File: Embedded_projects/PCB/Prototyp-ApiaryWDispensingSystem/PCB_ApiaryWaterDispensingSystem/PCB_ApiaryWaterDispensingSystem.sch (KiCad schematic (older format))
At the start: 0 parts

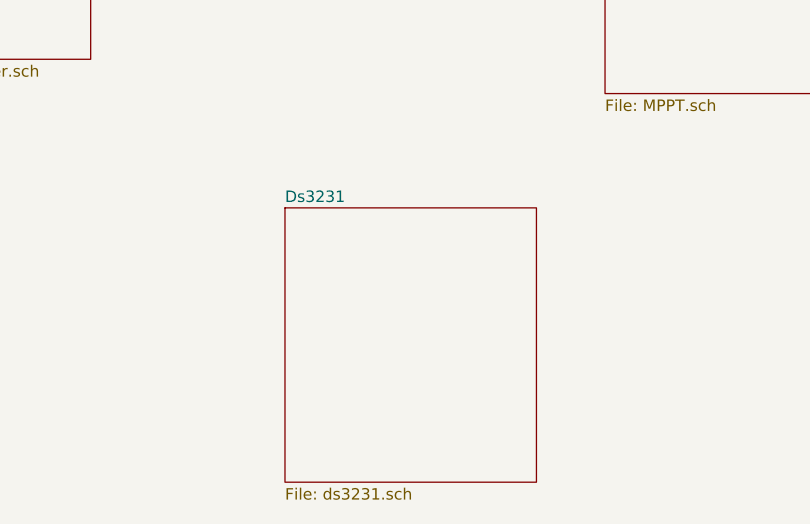
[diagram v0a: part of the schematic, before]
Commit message: added BME280 sensor to the project , #3
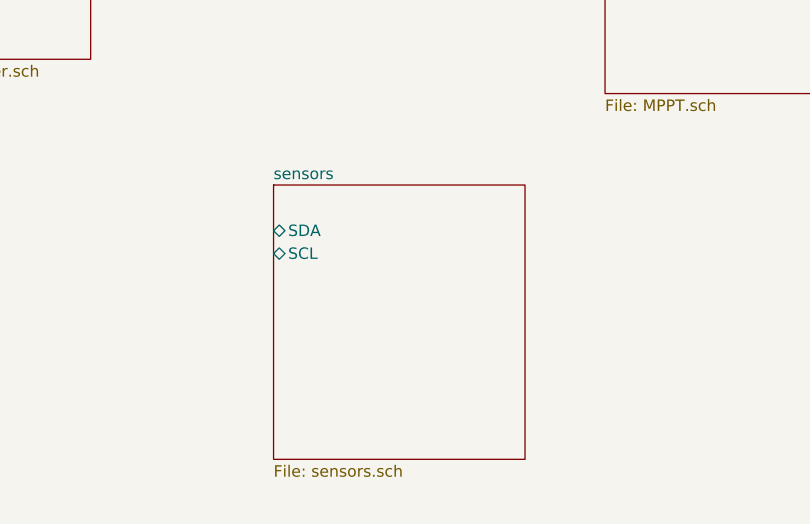
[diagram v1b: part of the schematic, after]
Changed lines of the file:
@@
 $EndSheet
 $Sheet
-S 4250 3850 1100 1200
+S 4200 3750 1100 1200
 U 67D47B32
-F0 "Ds3231" 50
-F1 "ds3231.sch" 50
+F0 "sensors" 50
+F1 "sensors.sch" 50
+F2 "SDA" B L 4200 3950 50
+F3 "SCL" B L 4200 4050 50
 $EndSheet
 $EndSCHEMATC

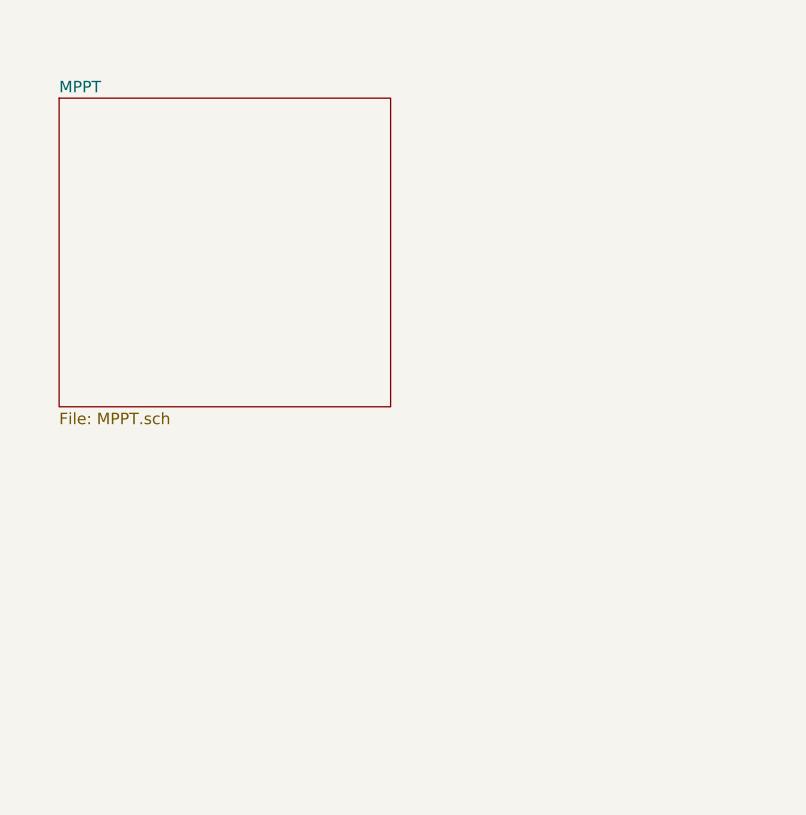
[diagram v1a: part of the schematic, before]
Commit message: added x-tal and his footprints for microcontroller schematics, user button
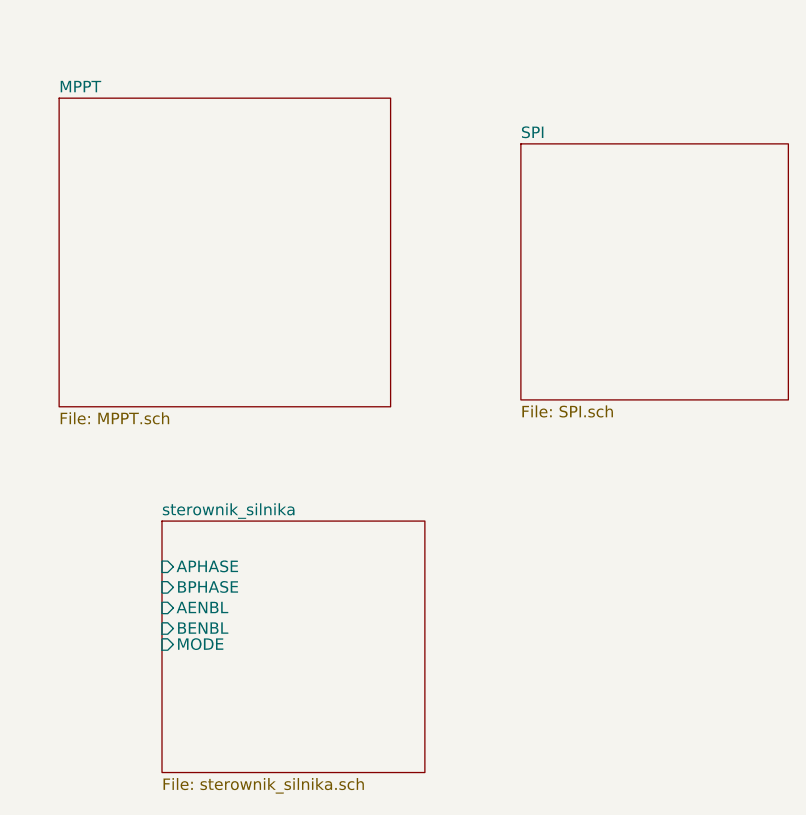
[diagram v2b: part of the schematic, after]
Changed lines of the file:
@@
 $Descr A4 11693 8268
 encoding utf-8
-Sheet 1 4
+Sheet 1 6
 Title ""
 Date ""
@@
 F3 "SCL" B L 4200 4050 50
 $EndSheet
+$Sheet
+S 6100 3850 1150 1100
+U 67E19E2D
+F0 "sterownik_silnika" 50
+F1 "sterownik_silnika.sch" 50
+F2 "APHASE" I L 6100 4050 50
+F3 "BPHASE" I L 6100 4140 50
+F4 "AENBL" I L 6100 4230 50
+F5 "BENBL" I L 6100 4320 50
+F6 "MODE" I L 6100 4390 50
+$EndSheet
+$Sheet
+S 7670 2200 1170 1120
+U 67E3C70E
+F0 "SPI" 50
+F1 "SPI.sch" 50
+$EndSheet
 $EndSCHEMATC

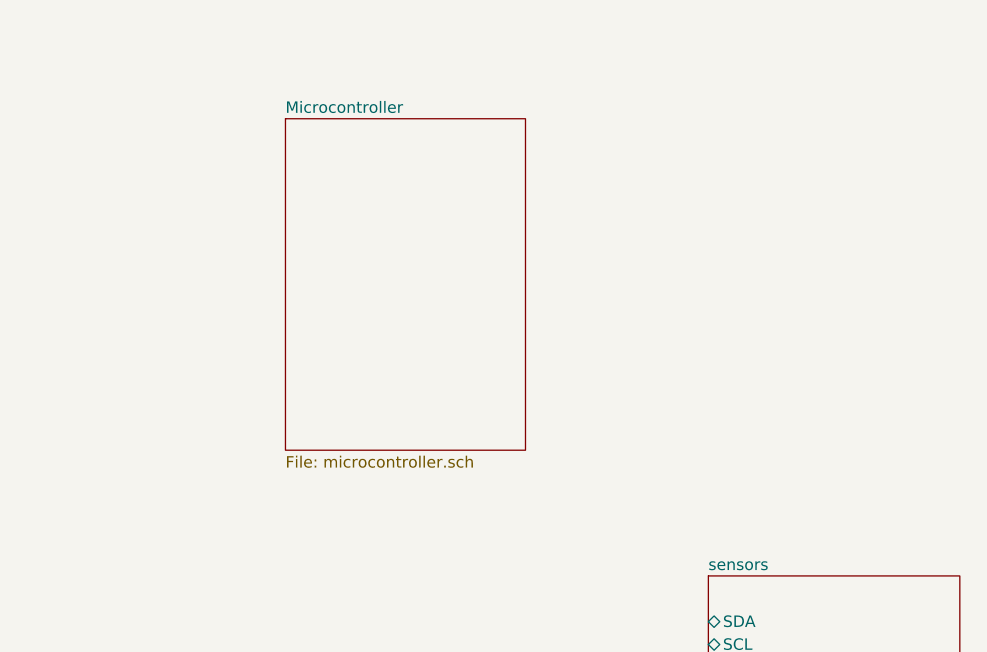
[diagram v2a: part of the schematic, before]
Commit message: stm32f411re completed schematic
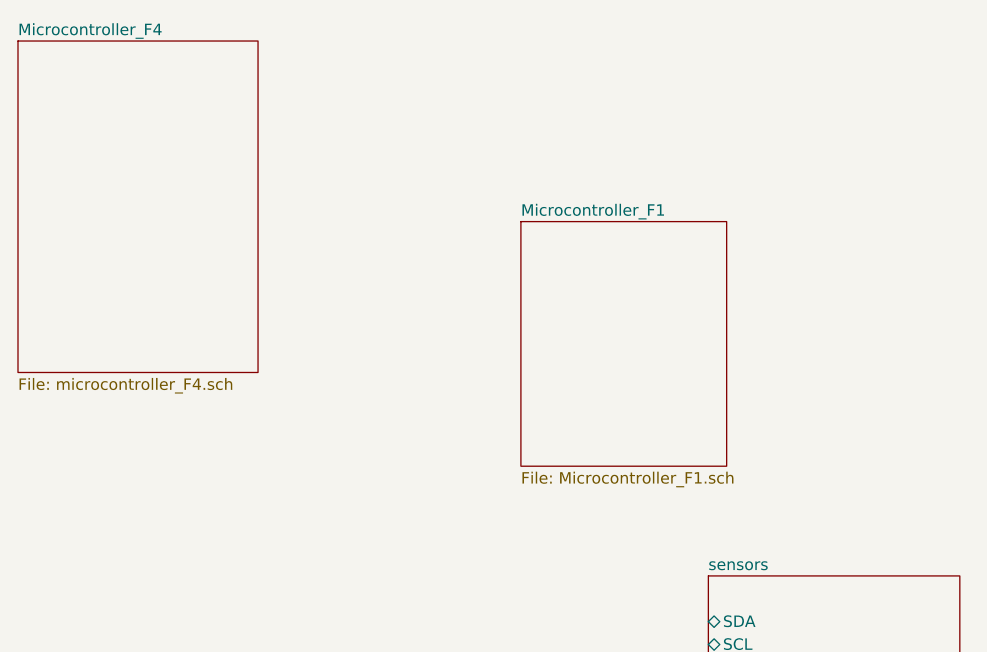
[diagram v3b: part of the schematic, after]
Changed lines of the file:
@@
 $Descr A4 11693 8268
 encoding utf-8
-Sheet 1 6
+Sheet 1 7
 Title ""
 Date ""
@@
 $EndDescr
 $Sheet
-S 2350 1750 1050 1450
+S 1180 1410 1050 1450
 U 67C77D26
-F0 "Microcontroller" 50
-F1 "microcontroller.sch" 50
+F0 "Microcontroller_F4" 50
+F1 "microcontroller_F4.sch" 50
 $EndSheet
 $Sheet
@@
 F1 "SPI.sch" 50
 $EndSheet
+$Sheet
+S 3380 2200 900  1070
+U 6818B51C
+F0 "Microcontroller_F1" 50
+F1 "Microcontroller_F1.sch" 50
+$EndSheet
 $EndSCHEMATC
